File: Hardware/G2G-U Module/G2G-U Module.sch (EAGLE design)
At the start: 3 parts, among them J1 GROVE-4P-2.0-3470130P1

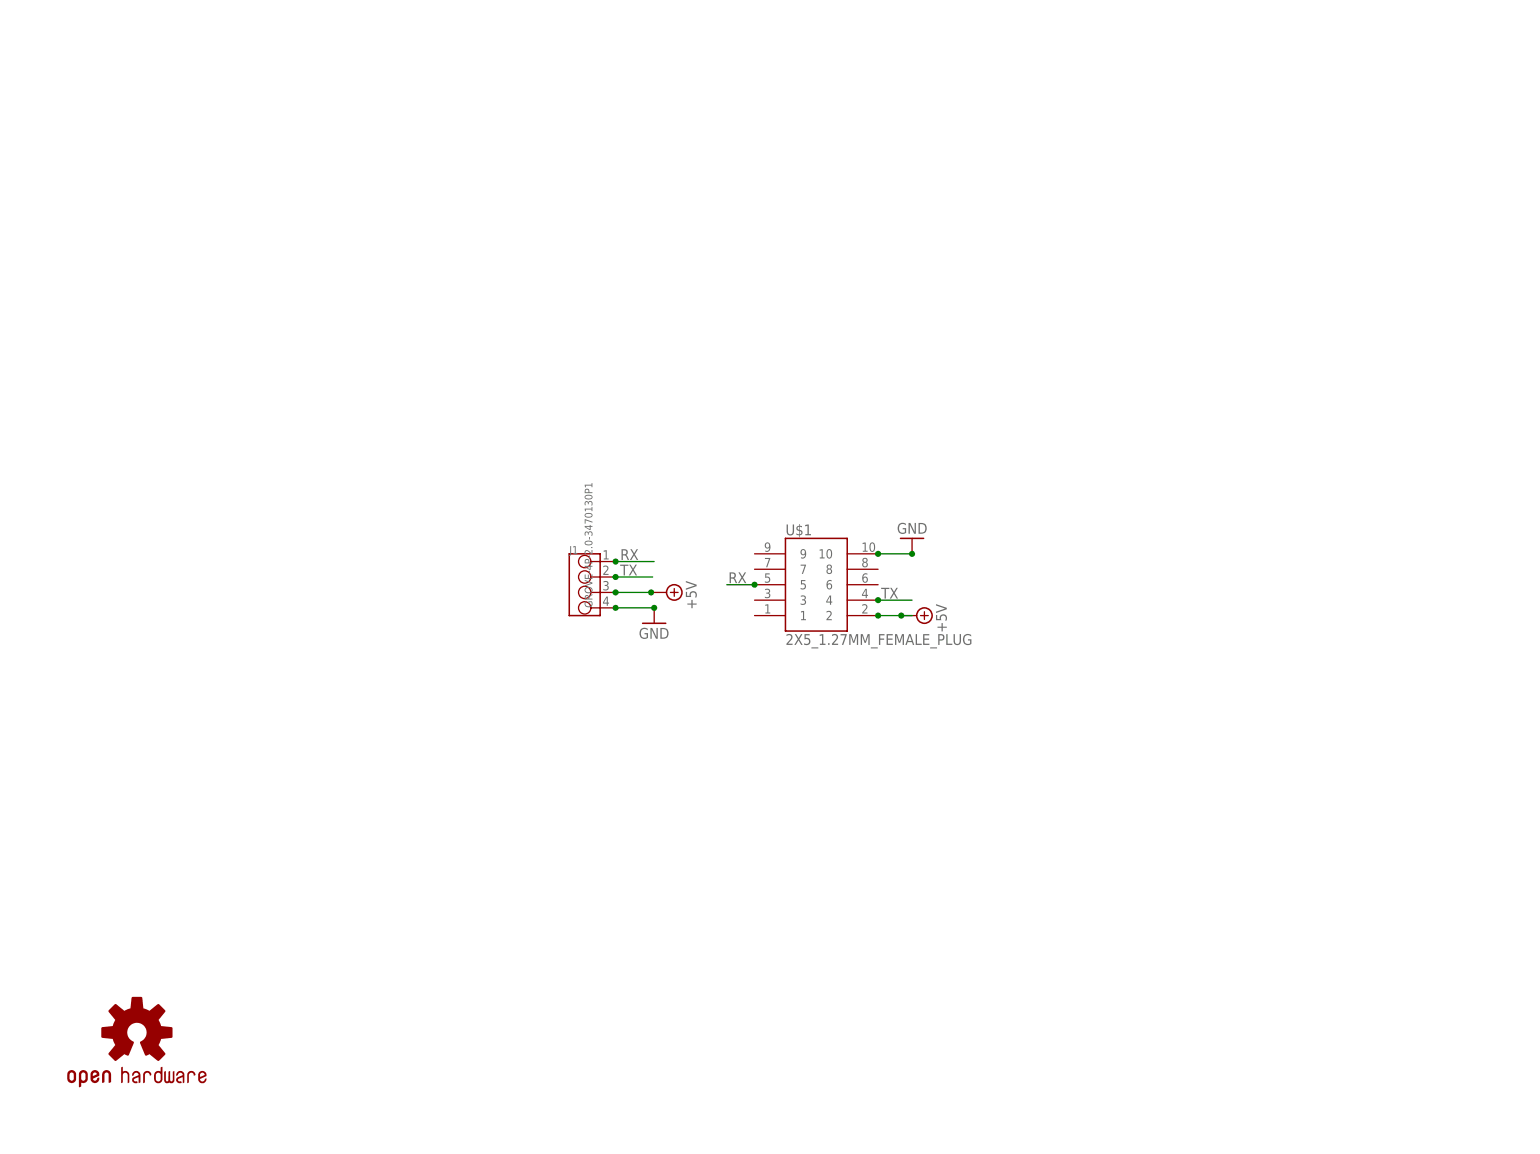
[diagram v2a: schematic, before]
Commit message: Added frames to the U and X module schematics.
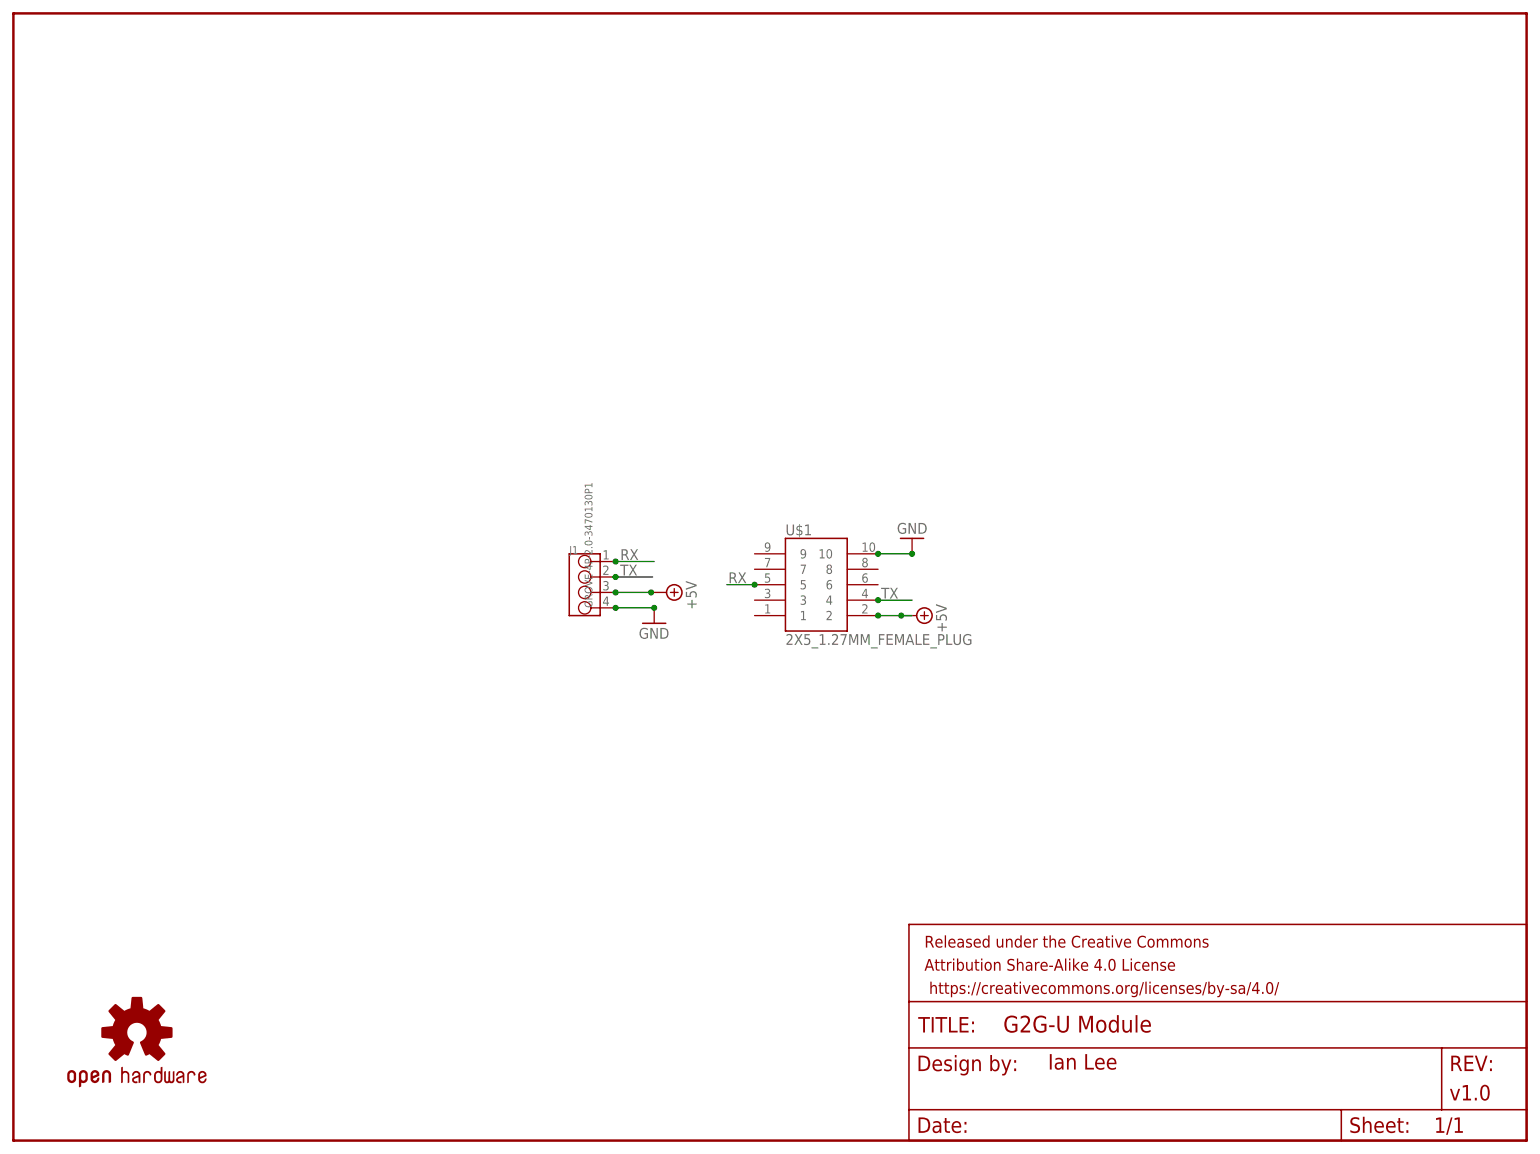
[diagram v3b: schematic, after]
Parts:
- added FRAME1: (no value), SparkFun-Aesthetics:FRAME-LETTERNO_PACKAGE
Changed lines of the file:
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@@
 <part name="SUPPLY1" library="supply2" deviceset="+5V" device=""/>
 <part name="SUPPLY2" library="supply2" deviceset="+5V" device=""/>
+<part name="FRAME1" library="SparkFun-Aesthetics" deviceset="FRAME-LETTER" device="NO_PACKAGE">
+<attribute name="DESIGNER" value="Ian Lee"/>
+<attribute name="VERSION" value="v1.0"/>
+</part>
 </parts>
 <sheets>
@@
 <instance part="SUPPLY1" gate="+5V" x="107.442" y="90.17" rot="R270"/>
 <instance part="SUPPLY2" gate="+5V" x="148.59" y="86.36" rot="R270"/>
+<instance part="FRAME1" gate="G$1" x="0" y="0"/>
+<instance part="FRAME1" gate="V" x="147.32" y="0"/>
 </instances>
 <busses>

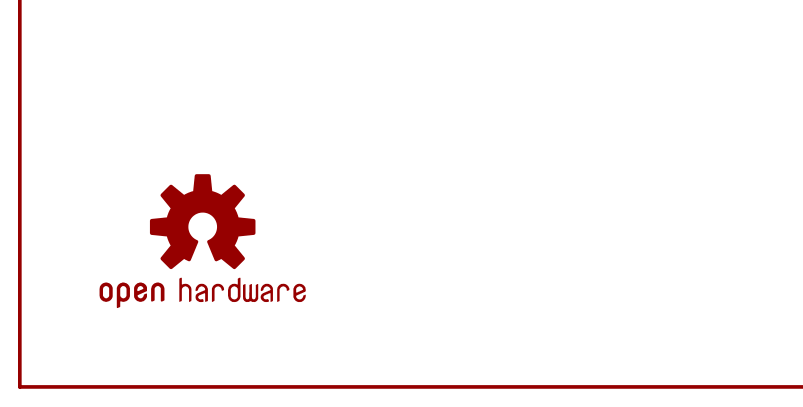
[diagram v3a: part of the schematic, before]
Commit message: Replaced all 'G' logos with a new part for the logo.
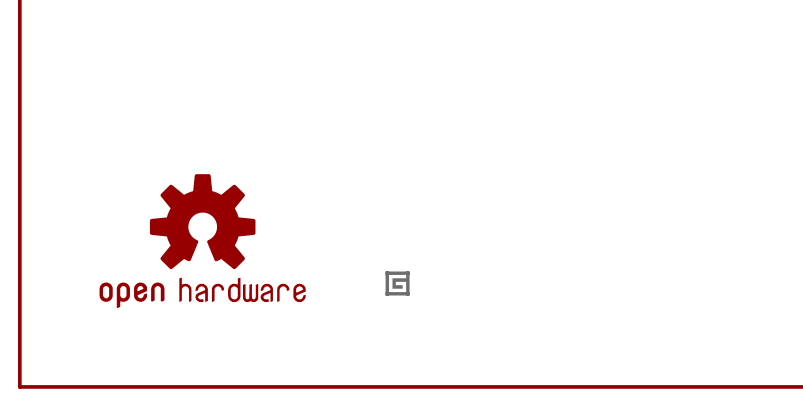
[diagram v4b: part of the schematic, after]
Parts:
- added U$2: GADGETEER_LOGO_SMALL, SoftDust:GADGETEER_LOGO_SMALL
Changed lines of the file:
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@@
 <attribute name="VERSION" value="v1.0"/>
 </part>
+<part name="U$2" library="SoftDust" deviceset="GADGETEER_LOGO_SMALL" device=""/>
 </parts>
 <sheets>
@@
 <instance part="FRAME1" gate="G$1" x="0" y="0"/>
 <instance part="FRAME1" gate="V" x="147.32" y="0"/>
+<instance part="U$2" gate="G$1" x="40.64" y="10.16"/>
 </instances>
 <busses>
